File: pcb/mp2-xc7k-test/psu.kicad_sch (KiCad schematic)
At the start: 116 parts, among them J1 BARREL_JACK, J2 CORTEX_DEBUG_ETM, J3 CONN_01X03, SW1 SWITCH, SW2 SWITCH, U1 LTC3374-QFN, U13 TCA6424A, U14 NCP45525IMNTWG-H, U2 STM32L431-QFN48, U3 NCP45525IMNTWG-H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

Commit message: Continued layout, 454 unrouted
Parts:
- C13, C14, C18, C19: value C -> 4.7 uF; footprint (none) -> azonenberg_pcb:EIA_0603_CAP_NOSILK
- R12, R13, R15, R16, R17, R18, R19, R2, R20, R21, R22: footprint (none) -> azonenberg_pcb:EIA_0402_RES_NOSILK
- U13: footprint (none) -> azonenberg_pcb:QFN_32_0.5MM_5x5MM
- U2: footprint (none) -> azonenberg_pcb:QFN_48_0.5MM_7x7MM
- U6, U8: footprint (none) -> azonenberg_pcb:SOT223-4
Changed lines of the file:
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@@
 			)
 		)
-		(property "Footprint" ""
+		(property "Footprint" "azonenberg_pcb:EIA_0402_RES_NOSILK"
 			(at 177.292 100.33 90)
 			(effects
@@
 			)
 		)
-		(property "Footprint" ""
+		(property "Footprint" "azonenberg_pcb:EIA_0402_RES_NOSILK"
 			(at 168.402 162.56 90)
 			(effects
@@
 			)
 		)
-		(property "Footprint" ""
+		(property "Footprint" "azonenberg_pcb:QFN_48_0.5MM_7x7MM"
 			(at 46.99 187.96 0)
 			(effects
@@
 			)
 		)
-		(property "Value" "C"
+		(property "Value" "4.7 uF"
 			(at 98.171 60.9021 0)
 			(effects
@@
 			)
 		)
-		(property "Footprint" ""
+		(property "Footprint" "azonenberg_pcb:EIA_0603_CAP_NOSILK"
 			(at 96.2152 63.5 0)
 			(effects
@@
 			)
 		)
-		(property "Footprint" ""
+		(property "Footprint" "azonenberg_pcb:EIA_0402_RES_NOSILK"
 			(at 168.402 30.48 90)
 			(effects
@@
 			)
 		)
-		(property "Footprint" ""
+		(property "Footprint" "azonenberg_pcb:EIA_0402_RES_NOSILK"
 			(at 168.402 198.12 90)
 			(effects
@@
 			)
 		)
-		(property "Footprint" ""
+		(property "Footprint" "azonenberg_pcb:QFN_48_0.5MM_7x7MM"
 			(at 41.91 247.65 0)
 			(effects
@@
 			)
 		)
-		(property "Value" "C"
+		(property "Value" "4.7 uF"
 			(at 140.081 60.9021 0)
 			(effects
@@
 			)
 		)
-		(property "Footprint" ""
+		(property "Footprint" "azonenberg_pcb:EIA_0603_CAP_NOSILK"
 			(at 138.1252 63.5 0)
 			(effects
@@
 			)
 		)
-		(property "Footprint" ""
+		(property "Footprint" "azonenberg_pcb:EIA_0402_RES_NOSILK"
 			(at 276.352 156.21 90)
 			(effects
@@
 			)
 		)
-		(property "Footprint" ""
+		(property "Footprint" "azonenberg_pcb:EIA_0402_RES_NOSILK"
 			(at 168.402 172.72 90)
 			(effects
@@
 			)
 		)
-		(property "Footprint" ""
+		(property "Footprint" "azonenberg_pcb:EIA_0402_RES_NOSILK"
 			(at 168.402 20.32 90)
 			(effects
@@
 			)
 		)
-		(property "Footprint" ""
+		(property "Footprint" "azonenberg_pcb:EIA_0402_RES_NOSILK"
 			(at 276.352 146.05 90)
 			(effects
@@
 			)
 		)
-		(property "Footprint" ""
+		(property "Footprint" "azonenberg_pcb:SOT223-4"
 			(at 114.3 46.99 0)
 			(effects
@@
 					(size 1.524 1.524)
 				)
+				(hide yes)
 			)
 		)
@@
 			)
 		)
-		(property "Footprint" ""
+		(property "Footprint" "azonenberg_pcb:SOT223-4"
 			(at 114.3 74.93 0)
 			(effects
@@
 					(size 1.524 1.524)
 				)
+				(hide yes)
 			)
 		)
@@
 			)
 		)
-		(property "Footprint" ""
+		(property "Footprint" "azonenberg_pcb:QFN_32_0.5MM_5x5MM"
 			(at 327.66 234.95 0)
 			(effects
@@
 					(size 1.524 1.524)
 				)
+				(hide yes)
 			)
 		)
@@
 			)
 		)
-		(property "Value" "C"
+		(property "Value" "4.7 uF"
 			(at 98.171 88.8421 0)
 			(effects
@@
 			)
 		)
-		(property "Footprint" ""
+		(property "Footprint" "azonenberg_pcb:EIA_0603_CAP_NOSILK"
 			(at 96.2152 91.44 0)
 			(effects
@@
 			)
 		)
-		(property "Footprint" ""
+		(property "Footprint" "azonenberg_pcb:EIA_0402_RES_NOSILK"
 			(at 177.292 110.49 90)
 			(effects
@@
 			)
 		)
-		(property "Value" "C"
+		(property "Value" "4.7 uF"
 			(at 140.081 88.8421 0)
 			(effects
@@
 			)
 		)
-		(property "Footprint" ""
+		(property "Footprint" "azonenberg_pcb:EIA_0603_CAP_NOSILK"
 			(at 138.1252 91.44 0)
 			(effects
@@
 			)
 		)
-		(property "Footprint" ""
+		(property "Footprint" "azonenberg_pcb:EIA_0402_RES_NOSILK"
 			(at 39.37 168.148 90)
 			(effects
@@
 			)
 		)
-		(property "Footprint" ""
+		(property "Footprint" "azonenberg_pcb:QFN_48_0.5MM_7x7MM"
 			(at 46.99 129.54 0)
 			(effects
@@
 			)
 		)
-		(property "Footprint" ""
+		(property "Footprint" "azonenberg_pcb:EIA_0402_RES_NOSILK"
 			(at 168.402 187.96 90)
 			(effects
@@
 			)
 		)
-		(property "Footprint" ""
+		(property "Footprint" "azonenberg_pcb:QFN_48_0.5MM_7x7MM"
 			(at 46.99 175.26 0)
 			(effects
@@
 			)
 		)
-		(property "Footprint" ""
+		(property "Footprint" "azonenberg_pcb:QFN_48_0.5MM_7x7MM"
 			(at 46.99 198.12 0)
 			(effects

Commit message: 111 unrouted, getting close
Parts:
- removed C28, C41: 10 uF, azonenberg_pcb:EIA_1210_CAP_NOSILK, symbol device:C
- removed R27: 10K, azonenberg_pcb:EIA_0402_RES_NOSILK, symbol device:R
- C24, C38: value 10 uF -> 22 uF
- TP10: value CONN_01X03 -> CONN_01X05; footprint azonenberg_pcb:CONN_HEADER_2.54MM_1x3 -> azonenberg_pcb:CONN_HEADER_2.54MM_1x5_REFLOW
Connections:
- net 1V2: now also U2.16 (PA6); no longer U2.12 (PA2)
- net 1V8: now also U2.17 (PA7); no longer U2.11 (PA1)
- net 1V8_2: now also U2.10 (PA0); no longer U2.18 (PB0)
- net 3V3: now also U2.11 (PA1); no longer U2.10 (PA0)
- net 3V3_RAW: now also L2.2; no longer L2.1
- net 5V0: now also C27.1, C29.1, C31.1
- net FPGA_DONE: now also U2.21 (PB10); no longer U2.2 (PC13)
- net FPGA_PROG_B: now also U2.6 (PH1); no longer U2.21 (PB10)
- net GND: now also C27.2, C29.2, C31.2
- net GTX_1V0: now also U2.18 (PB0); no longer U2.17 (PA7)
- net GTX_1V0_EN: now also U2.2 (PC13); no longer U2.6 (PH1)
- net LTC_VTEMP: now also U2.12 (PA2); no longer U2.16 (PA6)
- net SOC_BOOT0: now also U13.7 (P06); no longer U13.1 (P00)
- net SOC_BOOT1: now also U13.6 (P05); no longer U13.2 (P01)
- net SOC_BOOT2: now also U13.5 (P04); no longer U13.3 (P02)
- net SOC_NRST1CMS: now also U13.3 (P02); no longer U13.5 (P04)
- net SOC_PWR_CPU_ON: now also U13.11 (P12); no longer U2.3 (PC14)
- net SOC_PWR_LP: now also U13.9 (P10); no longer U2.4 (PC15)
- net SOC_PWR_ON: now also U13.10 (P11); no longer U2.20 (PB2)
- net SOC_RST_N: now also U13.8 (P07); no longer U2.45 (PB8)
- net SOFT_POWER: now also U13.15 (P16); no longer U2.25 (PB12)
- net SOFT_RESET: now also U13.16 (P17); no longer U2.28 (PB15)
- net SUPER_FAULT_LED: now also U13.21 (P24); no longer U13.18 (P21)
- net at U1.3 (SW1): now also L2.1; no longer L2.2
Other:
- moved on the sheet: C27, C29, C31, L2

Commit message: Test board ready for design review
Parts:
- removed R28, R29, R46: 10K, azonenberg_pcb:EIA_0402_RES_NOSILK, symbol device:R
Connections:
- net 0V82: now also U2.13 (PA3); no longer U2.15 (PA5)
- net 0V82_EN: now also U2.33 (PA12); no longer U2.19 (PB1)
- net 0V9_EN: now also U13.23 (P26); no longer U2.33 (PA12)
- net 1V0: now also U2.15 (PA5); no longer U2.13 (PA3)
- net 1V2_EN: now also U2.5 (PH0); no longer U2.29 (PA8)
- net 1V8_2: now also U2.12 (PA2); no longer U2.10 (PA0)
- net 1V8_EN: now also U13.22 (P25); no longer U2.5 (PH0)
- net 3V3_RAW: now also L2.1; no longer L2.2
- net GND: now also U13.PAD (GND)
- net GTX_1V0_EN: now also U13.24 (P27); no longer U2.2 (PC13)
- net LTC_VTEMP: now also U2.10 (PA0); no longer U2.12 (PA2)
- net SOC_BOOT0: now also U13.9 (P10); no longer U13.7 (P06)
- net SOC_BOOT1: now also U13.8 (P07); no longer U13.6 (P05)
- net SOC_BOOT2: now also U13.7 (P06); no longer U13.5 (P04)
- net SOC_BOOT3: now also U13.6 (P05); no longer U13.4 (P03)
- net SOC_NRST1CMS: now also U13.5 (P04); no longer U13.3 (P02)
- net SOC_PWR_CPU_ON: now also U13.3 (P02); no longer U13.11 (P12)
- net SOC_PWR_LP: now also U13.1 (P00); no longer U13.9 (P10)
- net SOC_PWR_ON: now also U13.2 (P01); no longer U13.10 (P11)
- net SOC_RST_N: now also U13.10 (P11); no longer U13.8 (P07)
- net at U1.3 (SW1): now also L2.2; no longer L2.1
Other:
- note added: "TODO: validate that VCCINT inductor can handle the current"
- moved on the sheet: L1, L2

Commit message: Changed L1 to larger, higher current NRS5030. Reduced inductance from 2.2 uH to 1 per datasheet recommendations
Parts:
- L1: value 2.2 uH -> 1 uH; footprint azonenberg_pcb:EIA_1210_CAP_NOSILK -> azonenberg_pcb:INDUCTOR_YUDEN_NRS5030
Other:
- note added: "Original design called for DFE322520FD-2R2M=P2 Thermals are marginal at worst case current but should be fine w/ realistic load But if we can fit, NRS5030 is better We have it in 1 uH"
- note removed: "TODO: validate that VCCINT inductor can handle the current"
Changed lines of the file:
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@@
 		)
 	)
-	(text "TODO: validate that VCCINT inductor can handle the current"
+	(text "Original design called for \nDFE322520FD-2R2M=P2\nThermals are marginal at worst\ncase current but should be fine\nw/ realistic load\n\nBut if we can fit, NRS5030 is better\nWe have it in 1 uH"
 		(exclude_from_sim no)
-		(at 328.93 88.9 0)
+		(at 146.05 127 0)
 		(effects
 			(font
 				(size 1.27 1.27)
 			)
+			(justify left)
 		)
 	)
@@
 	(polyline
 		(pts
-			(xy 78.74 66.04) (xy -29.21 66.04)
+			(xy 78.74 66.04) (xy 186.69 66.04)
 		)
 		(stroke
@@
 		(dnp no)
 		(property "Reference" "L2"
-			(at 152.4 31.3447 90)
+			(at 152.4 24.13 90)
 			(effects
 				(font
@@
 		)
 		(property "Value" "2.2 uH"
-			(at 152.4 29.3292 90)
+			(at 152.4 22.1145 90)
 			(effects
 				(font
@@
 			)
 		)
-		(property "Value" "2.2 uH"
+		(property "Value" "1 uH"
 			(at 152.4 102.87 90)
 			(effects
@@
 			)
 		)
-		(property "Footprint" "azonenberg_pcb:EIA_1210_CAP_NOSILK"
+		(property "Footprint" "azonenberg_pcb:INDUCTOR_YUDEN_NRS5030"
 			(at 152.4 106.68 0)
 			(effects

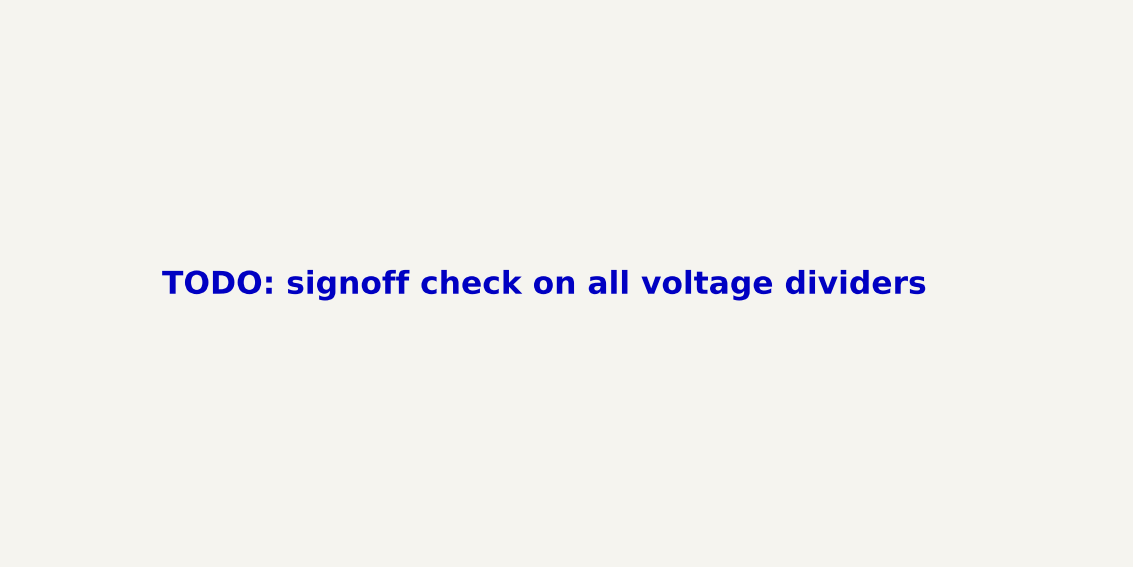
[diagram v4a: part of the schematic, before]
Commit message: Schematic review complete, added a few more test points
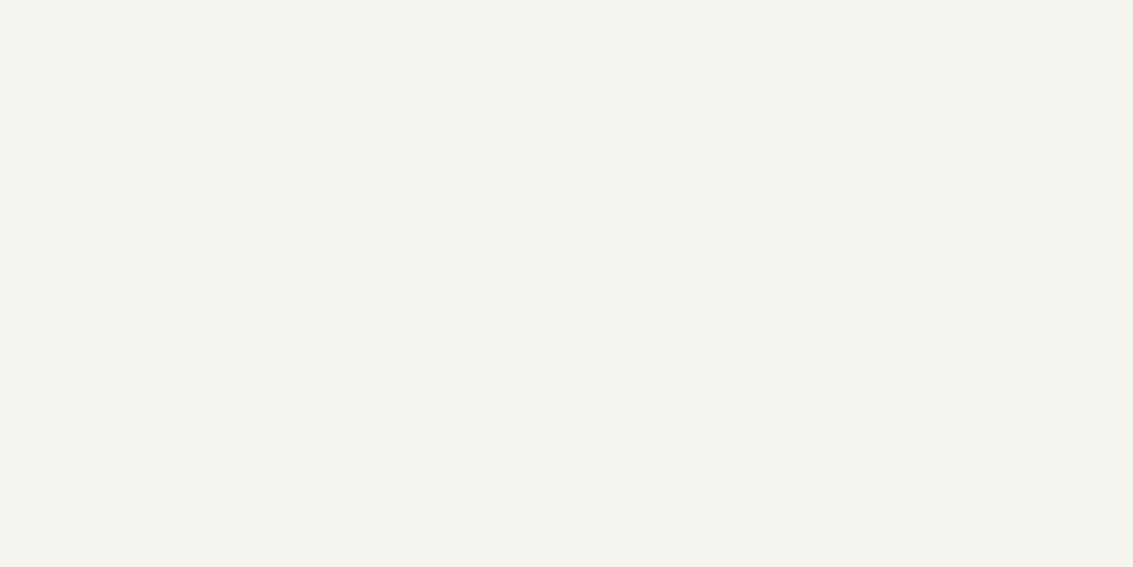
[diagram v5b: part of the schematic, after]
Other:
- note removed: "TODO: signoff check on all voltage dividers"
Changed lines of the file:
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@@
-		)
-	)
-	(text "TODO: signoff check on all voltage dividers"
-		(exclude_from_sim no)
-		(at 311.15 78.74 0)
-		(effects
-			(font
-				(size 2.54 2.54)
-				(thickness 0.508)
-				(bold yes)
-			)
-			(justify left)
 		)
 	)

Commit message: Added 1V8_SOC load switch
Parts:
- added C141: 0.47 uF, azonenberg_pcb:EIA_0402_CAP_NOSILK, symbol device:C
- added C28: DNP, azonenberg_pcb:EIA_0402_CAP_NOSILK, symbol device:C
- added C41: 4.7 uF, azonenberg_pcb:EIA_0603_CAP_NOSILK, symbol device:C
- added R27: 10K, azonenberg_pcb:EIA_0402_RES_NOSILK, symbol device:R
- added U19: NCP45525IMNTWG-H, azonenberg_pcb:DFN_8_0.5MM_2x2MM, symbol power-azonenberg:NCP45525
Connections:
- net 1V8_2: now also U19.1 (VIN), U19.PAD (VIN)
- net 3V3: now also C141.1, U19.3 (VCC)
- net GND: now also C141.2, C28.2, C41.2, R27.2, U19.4 (GND)
- net SOC_1V8_EN: now reaches U2.3 (PC14)
- net SOC_1V8_EN: now also R27.1, U19.2 (EN)
- new net: C28.1, U19.6 (SR)
- new net SOC_1V8: C41.1, U19.5 (BLEED), U19.7 (VOUT), U19.8 (VOUT)
- no-connect marks 25 -> 24
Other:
- note added: "OK to feed this from 3V3 not 3V3_RAW * NCP45525 is OK with VCC/VIN in any order * 1V8_2 and 3V3 ramp simultaneously * SOC_1V8_EN always comes after 3V3 and 1V8_2 stable"
- note added: "SoC 1V8 load switch"
